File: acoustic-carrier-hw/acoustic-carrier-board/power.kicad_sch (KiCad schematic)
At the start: 79 parts, among them IC1 ECP5-BGA256, J7 Conn_02x04_Odd_Even, U10 TLV62569DRL, U11 TLV62569DRL, U12 TLV62569DRL, U8 TLV62569DRL

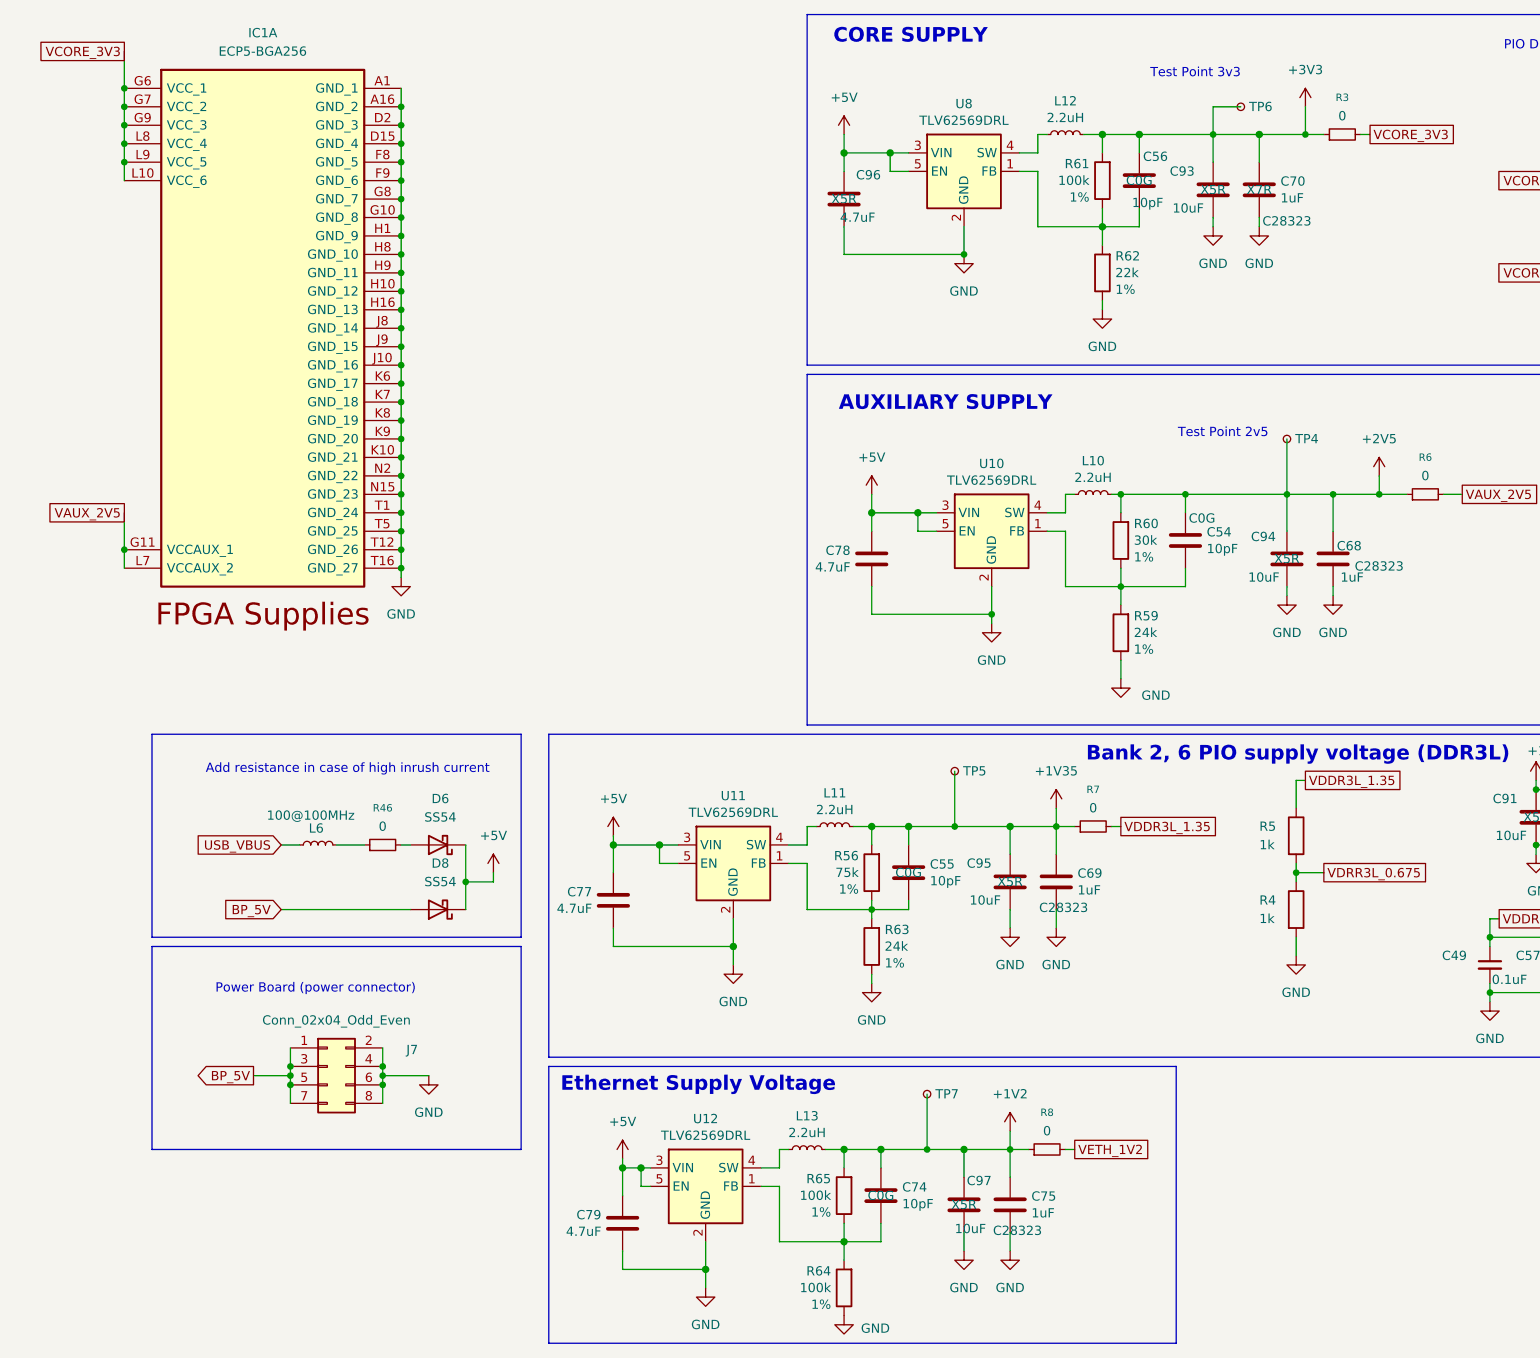
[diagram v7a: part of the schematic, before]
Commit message: [carrier] Reorganized carrier board schematic, added lcsc part numbers (next) check schematic before component placement
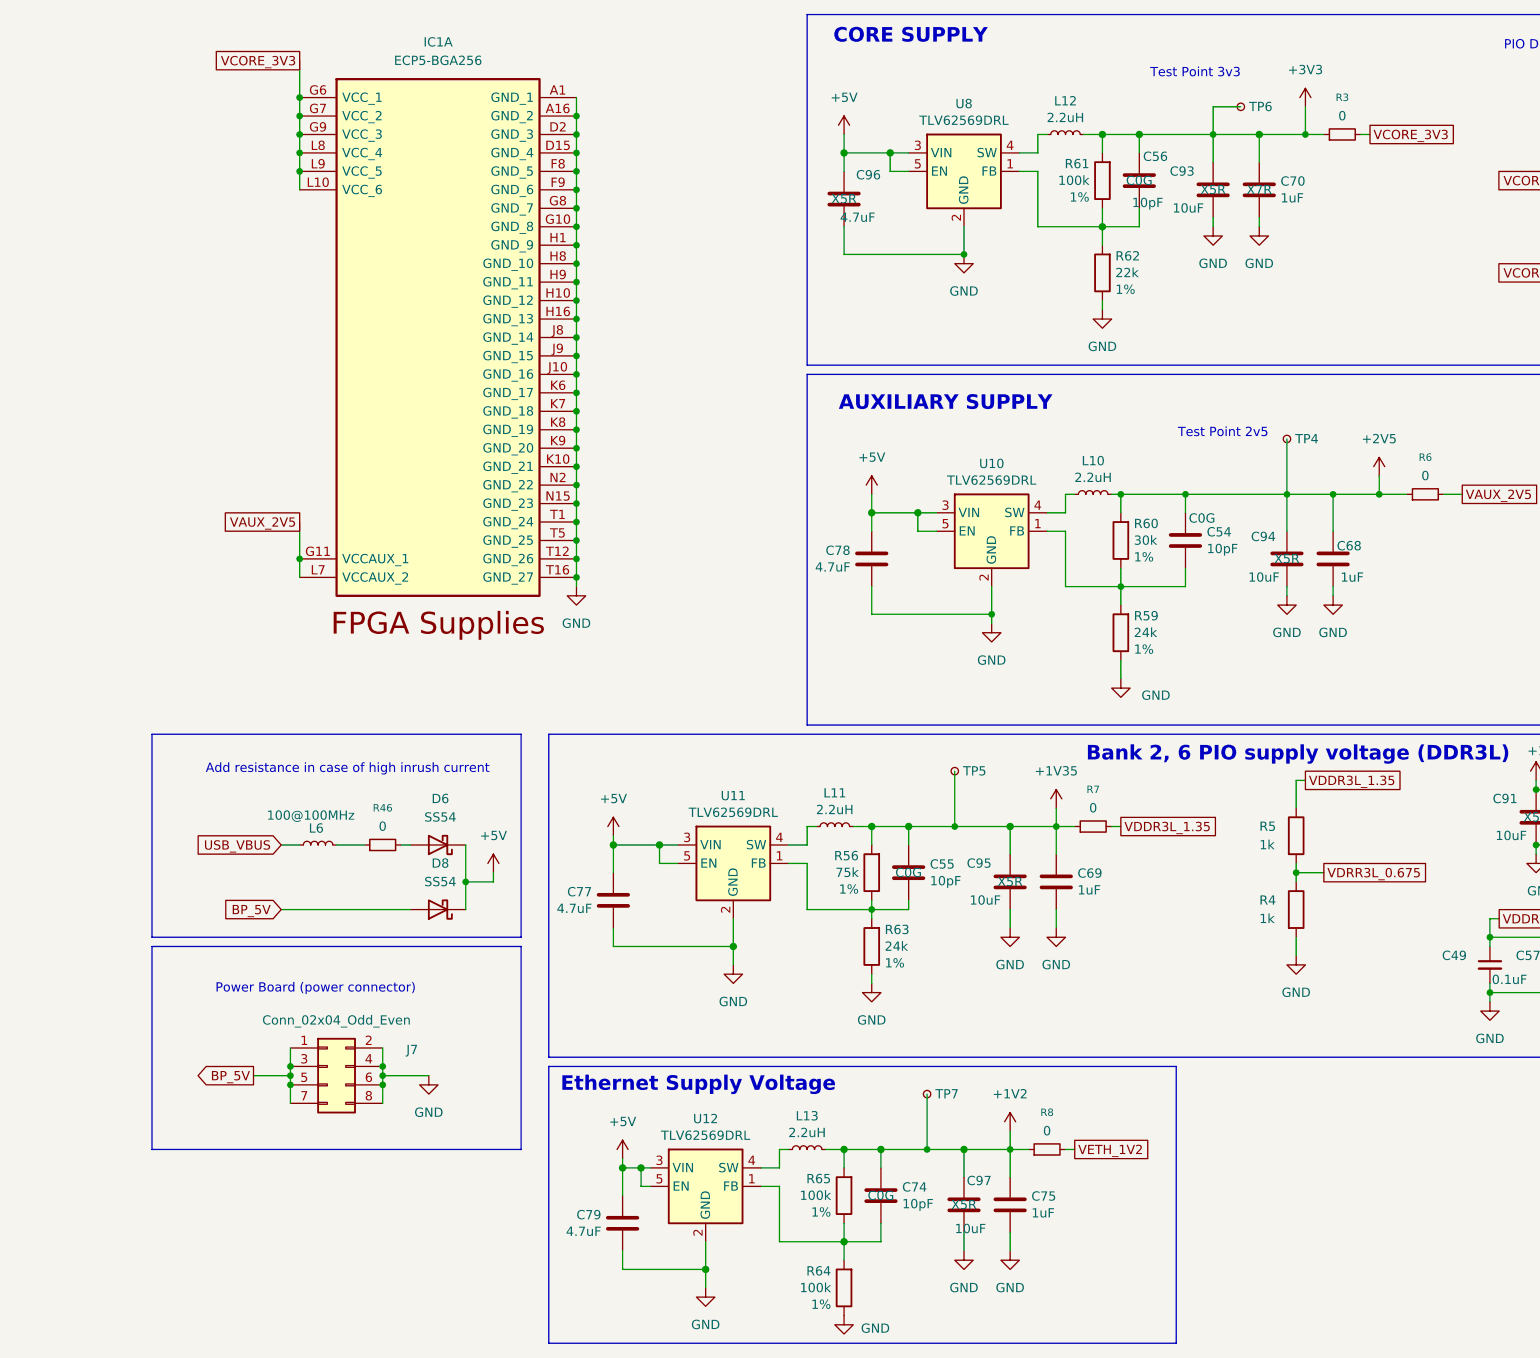
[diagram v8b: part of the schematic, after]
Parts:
- C33, C36, C45, C48, C49, C50, C51, C52, C57, C58, C59, C61, C62, C63, C64, C65, C66, C67, C72: LCSC Part Number C307331 -> (none); LPN (none) -> C307331; MPN (none) -> CL05B104KB54PNC; Manufacturing Part Number CL05B104KB54PNC -> (none)
- C53, C60: LCSC Part Number C1623 -> (none); LPN (none) -> C1623; MPN (none) -> CL10B474KA8NNNC; Manufacturing Part Number CL10B474KA8NNNC -> (none)
- C68, C69, C70, C75: LCSC Part Number C28323 -> (none); LPN (none) -> C28323; MPN (none) -> CL21B105KBFNNNE; Manufacturing Part Number CL21B105KBFNNNE -> (none)
- C71, C73: LCSC Part Number C1524 -> (none); LPN (none) -> CL05B103KB5NNNC; MPN (none) -> C15195; Manufacturing Part Number 0402B103K500NT -> (none)
- C85: LCSC Part Number C16780 -> (none); LPN (none) -> C16780; MPN (none) -> CL21A476MQYNNNE; Manufacturing Part Number CL21A476MQYNNNE -> (none)
- C86, C87, C88, C89, C91, C92, C93, C94, C95, C97: LCSC Part Number C19702 -> (none); LPN (none) -> C19702; MPN (none) -> CL10A106KP8NNNC; Manufacturing Part Number CL10A106KP8NNNC -> (none)
- C90, C96: LCSC Part Number C23733 -> (none); LPN (none) -> C23733; MPN (none) -> CL05A475MP5NRNC; Manufacturing Part Number CL05A475MP5NRNC -> (none)
- L10, L11, L12, L13: LCSC Part Number C28642347 -> (none); LPN (none) -> C28642347; MPN (none) -> NR4018S2R2MT; Manufacturing Part Number NR4018S2R2MT -> (none)
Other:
- moved on the sheet: IC1A
